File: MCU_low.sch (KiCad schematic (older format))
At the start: 20 parts

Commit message: - MCU_Low: added encoder, DAC, alternate MCU
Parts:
- removed SW?: Rotary_Encoder_Switch, symbol Device:Rotary_Encoder_Switch
- added SW?: Rotary_Encoder_Switch, Rotary_Encoder:RotaryEncoder_Alps_EC12E-Switch_Vertical_H20mm_CircularMountingHoles, symbol Device:Rotary_Encoder_Switch
- added U?: LCD_I2C, symbol miscellaneous:LCD_I2C
- added U?: STM32F103C8Tx, Package_QFP:LQFP-48_7x7mm_P0.5mm, symbol MCU_ST_STM32F1:STM32F103C8Tx
- added U?: DAC8564, Package_SO:TSSOP-16_4.4x5mm_P0.65mm, symbol miscellaneous:DAC8564
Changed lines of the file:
@@
 $EndDescr
-$Comp
-L Device:Rotary_Encoder_Switch SW?
-U 1 1 5F7D692F
-P 2400 6850
-AR Path="/5F7D692F" Ref="SW?"  Part="1"
-AR Path="/5F7D6767/5F7D692F" Ref="SW?"  Part="1"
-F 0 "SW?" H 2400 7217 50  0000 C CNN
-F 1 "Rotary_Encoder_Switch" H 2400 7126 50  0000 C CNN
-F 2 "" H 2250 7010 50  0001 C CNN
-F 3 "~" H 2400 7110 50  0001 C CNN
-	1    2400 6850
-	1    0    0    -1
-$EndComp
 $Comp
 L MCU_Module:NUCLEO64-F411RE U?
@@
 $EndComp
 Connection ~ 8450 5300
+$Comp
+L miscellaneous:LCD_I2C U?
+U 1 1 5F8792B9
+P 8950 1200
+F 0 "U?" H 9579 1246 50  0000 L CNN
+F 1 "LCD_I2C" H 9579 1155 50  0000 L CNN
+F 2 "" H 8950 1200 50  0001 C CNN
+F 3 "" H 8950 1200 50  0001 C CNN
+	1    8950 1200
+	1    0    0    -1
+$EndComp
+$Comp
+L power:GND #PWR?
+U 1 1 5F879504
+P 8550 1500
+AR Path="/5F40DCB9/5F879504" Ref="#PWR?"  Part="1"
+AR Path="/5F618AB9/5F879504" Ref="#PWR?"  Part="1"
+AR Path="/5F879504" Ref="#PWR?"  Part="1"
+AR Path="/5F620813/5F879504" Ref="#PWR?"  Part="1"
+AR Path="/5F7D6767/5F879504" Ref="#PWR?"  Part="1"
+F 0 "#PWR?" H 8550 1340 50  0001 C CNN
+F 1 "GND" H 8550 1400 39  0000 C TNN
+F 2 "" H 8550 1500 50  0001 C CNN
+F 3 "" H 8550 1500 50  0001 C CNN
+	1    8550 1500
+	1    0    0    -1
+$EndComp
+$Comp
+L Device:Rotary_Encoder_Switch SW?
+U 1 1 5F87AEF8
+P 7700 1200
+AR Path="/5F87AEF8" Ref="SW?"  Part="1"
+AR Path="/5F7D6767/5F87AEF8" Ref="SW?"  Part="1"
+F 0 "SW?" H 7700 1567 50  0000 C CNN
+F 1 "Rotary_Encoder_Switch" H 7700 1476 50  0000 C CNN
+F 2 "Rotary_Encoder:RotaryEncoder_Alps_EC12E-Switch_Vertical_H20mm_CircularMountingHoles" H 7550 1360 50  0001 C CNN
+F 3 "~" H 7700 1460 50  0001 C CNN
+F 4 "PEC12R-4222F-S0024" H 7700 1200 50  0001 C CNN "Mfr. No"
+F 5 "4.33" H 7700 1200 50  0001 C CNN "Price [PLN]"
+	1    7700 1200
+	1    0    0    -1
+$EndComp
+$Comp
+L MCU_ST_STM32F1:STM32F103C8Tx U?
+U 1 1 5F87E496
+P 3050 2950
+F 0 "U?" H 3000 1364 50  0000 C CNN
+F 1 "STM32F103C8Tx" H 3000 1273 50  0000 C CNN
+F 2 "Package_QFP:LQFP-48_7x7mm_P0.5mm" H 2450 1550 50  0001 R CNN
+F 3 "http://www.st.com/st-web-ui/static/active/en/resource/technical/document/datasheet/CD00161566.pdf" H 3050 2950 50  0001 C CNN
+	1    3050 2950
+	1    0    0    -1
+$EndComp
+$Comp
+L miscellaneous:DAC8564 U?
+U 1 1 5F888149
+P 5500 6750
+F 0 "U?" H 5500 5814 50  0000 C CNN
+F 1 "DAC8564" H 5500 5723 50  0000 C CNN
+F 2 "Package_SO:TSSOP-16_4.4x5mm_P0.65mm" H 6500 5700 50  0001 C CNN
+F 3 "" H 6500 5700 50  0001 C CNN
+F 4 "44.7" H 5500 6750 50  0001 C CNN "Price [PLN]"
+	1    5500 6750
+	1    0    0    -1
+$EndComp
 $EndSCHEMATC

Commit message: - drivers modified - MCU replaced
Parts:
- removed C? (x7): 100n, Capacitor_SMD:C_0603_1608Metric_Pad1.05x0.95mm_HandSolder, symbol Device:C_Small
- removed U?: NUCLEO64-F411RE, Module:ST_Morpho_Connector_144_STLink, symbol MCU_Module:NUCLEO64-F411RE
- removed U?: STM32F103C8Tx, Package_QFP:LQFP-48_7x7mm_P0.5mm, symbol MCU_ST_STM32F1:STM32F103C8Tx
- removed U?: DAC8564, Package_SO:TSSOP-16_4.4x5mm_P0.65mm, symbol miscellaneous:DAC8564
- added C? (x7): 10n, Capacitor_SMD:C_0603_1608Metric_Pad1.05x0.95mm_HandSolder, symbol Device:C_Small
- added U?: STM32L431RBTx, Package_QFP:LQFP-64_10x10mm_P0.5mm, symbol MCU_ST_STM32L4:STM32L431RBTx
- C?: value 100n -> 10n
- SW?: footprint Rotary_Encoder:RotaryEncoder_Alps_EC12E-Switch_Vertical_H20mm_CircularMountingHoles -> miscellaneous_my:Encoder_12.4x13.4_pitch2.5mm_wSw
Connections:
- net labels added: +3V3, TIM1_CH1, TIM1_CH2, TIM1_CH3, TIM1_CH4, dac_1, dac_2, dac_3, dac_4
- net labels removed: dac_E, dac_F, dac_K
- wire segments 34 -> 58
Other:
- moved on the sheet: C?, R?

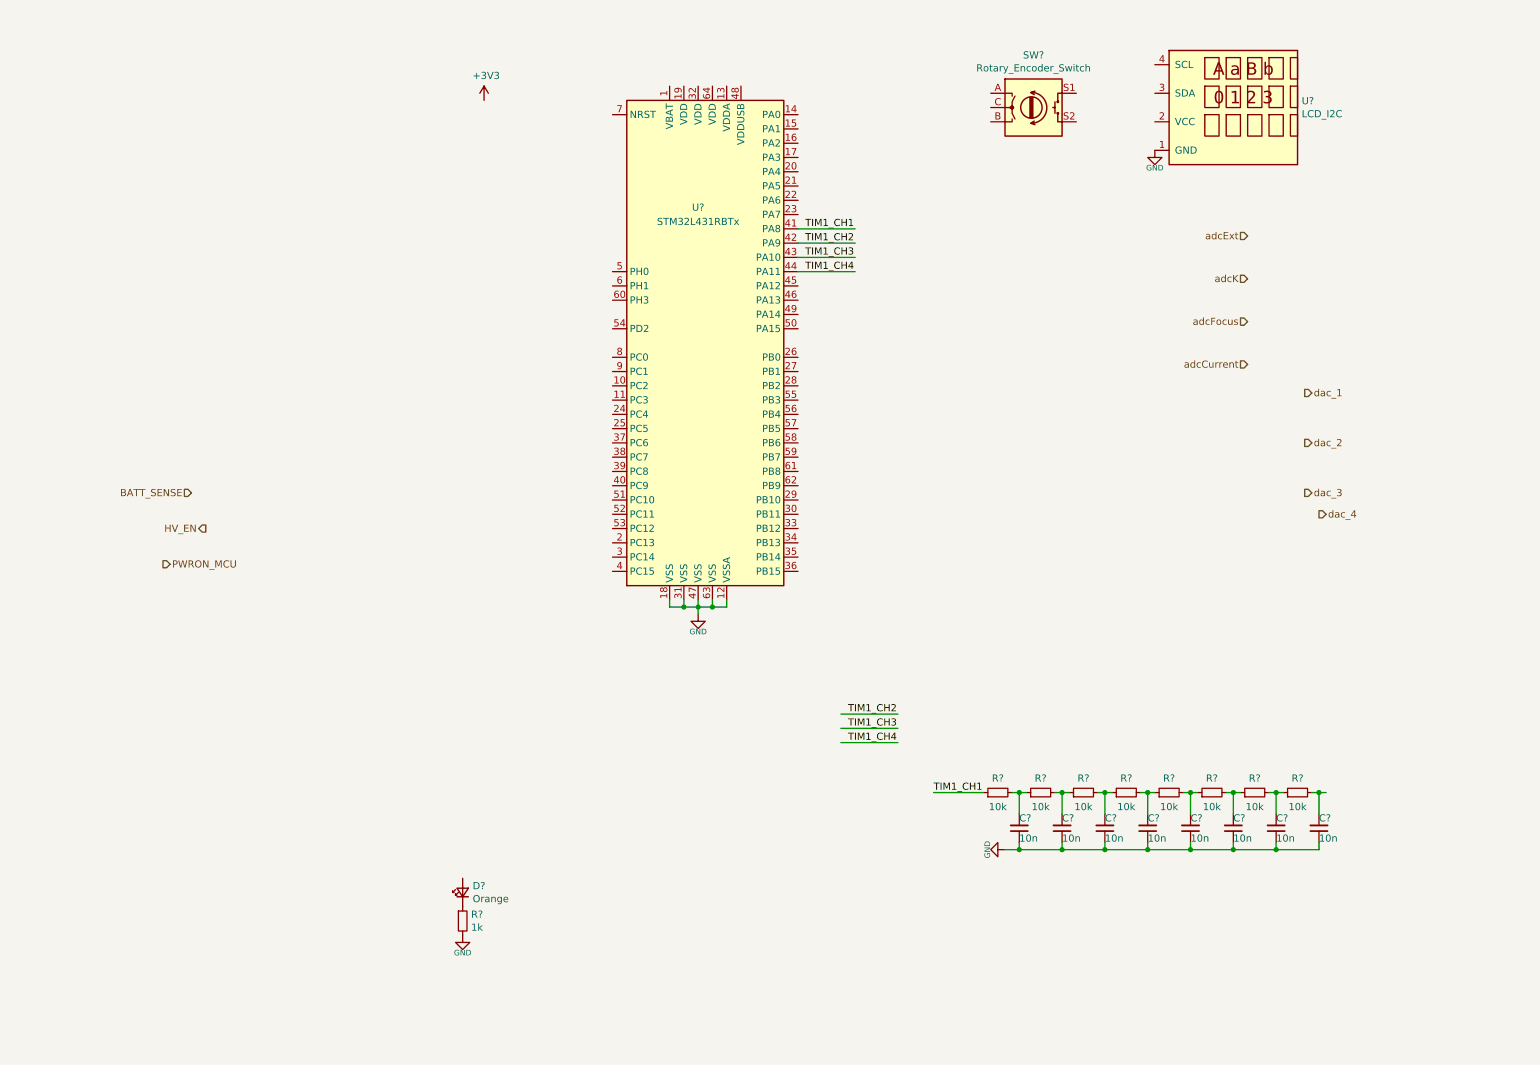
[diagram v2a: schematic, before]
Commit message: - connect things to MCUlow (DAC, screen, keys, debug) - improvement in charger (read PWR key)
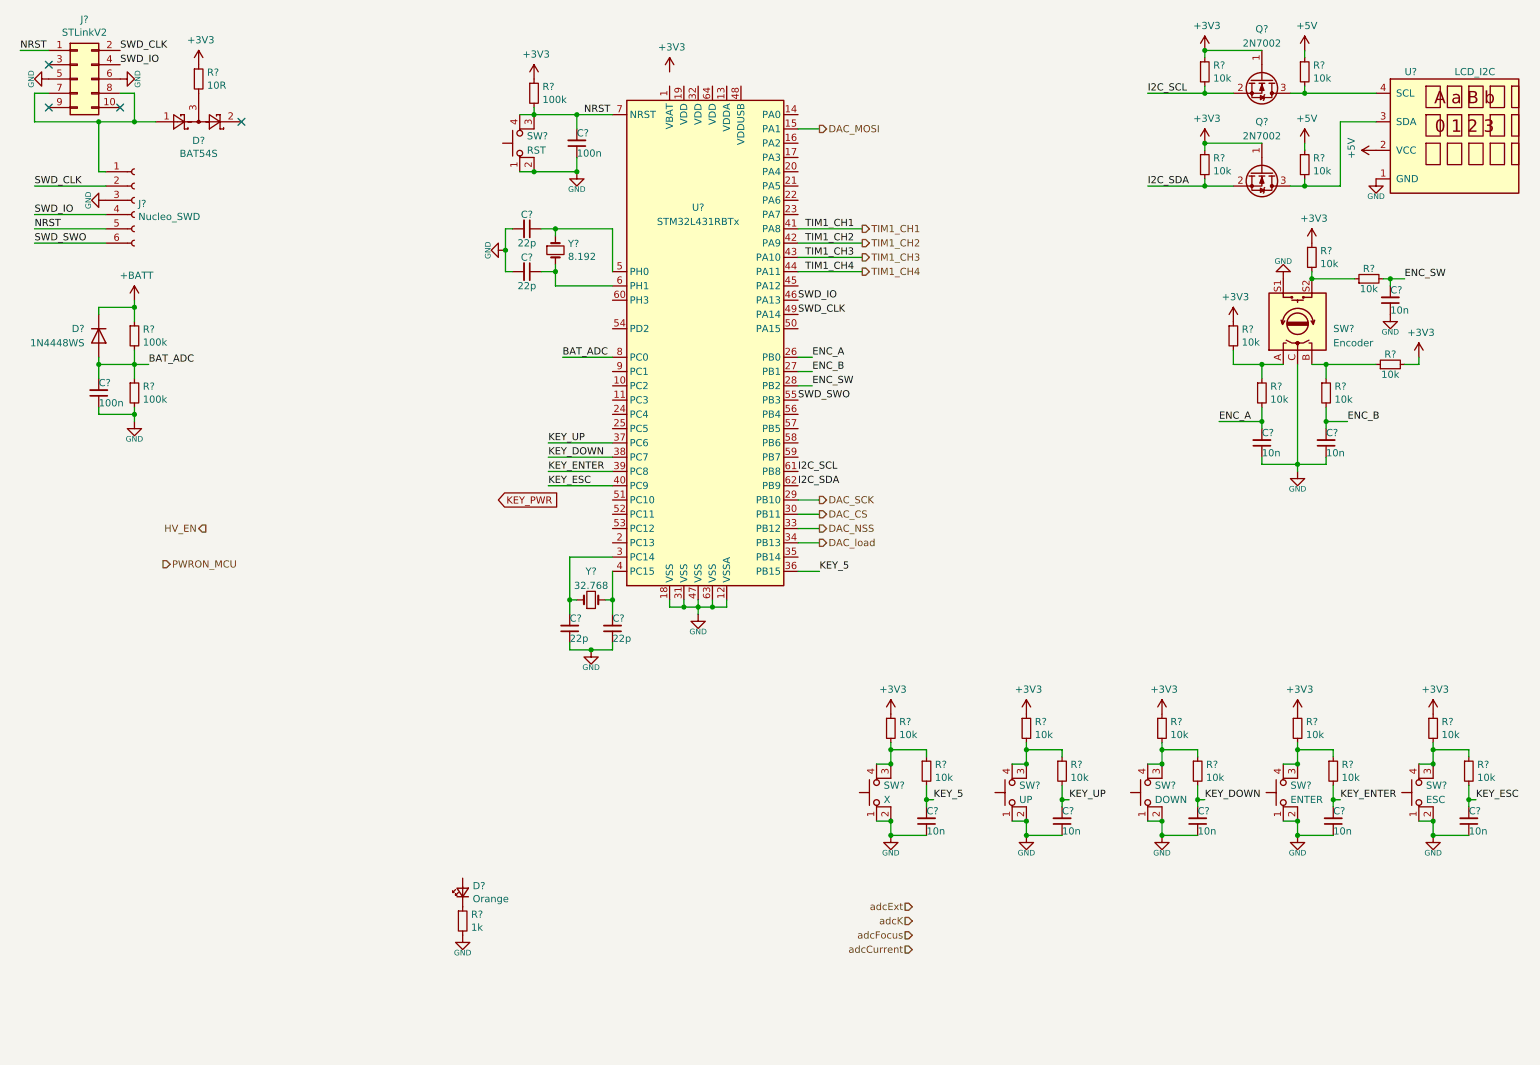
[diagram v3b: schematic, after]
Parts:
- removed C? (x8): 10n, Capacitor_SMD:C_0603_1608Metric_Pad1.05x0.95mm_HandSolder, symbol Device:C_Small
- removed R? (x8): 10k, Resistor_SMD:R_0603_1608Metric_Pad1.05x0.95mm_HandSolder, symbol Device:R_Small
- added C? (x2): 100n, Capacitor_SMD:C_0603_1608Metric_Pad1.05x0.95mm_HandSolder, symbol Device:C_Small
- added C? (x4): 22p, Capacitor_SMD:C_0603_1608Metric_Pad1.05x0.95mm_HandSolder, symbol Device:C_Small
- added C? (x8): 10n, Capacitor_SMD:C_0603_1608Metric_Pad1.05x0.95mm_HandSolder, symbol Device:C_Small
- added D?: BAT54S, Package_TO_SOT_SMD:SOT-23, symbol Diode:BAT54S
- added D?: 1N4448WS, Diode_SMD:D_SOD-323, symbol Diode:1N4448WS
- added J?: STLinkV2, miscellaneous_my:ST-LinkV2_FakeStm8Stm32_vertical, symbol Connector_Generic:Conn_02x05_Odd_Even
- added J?: Nucleo_SWD, Connector_PinSocket_2.54mm:PinSocket_1x06_P2.54mm_Vertical, symbol Connector:Conn_01x06_Female
- added Q? (x2): 2N7002, Package_TO_SOT_SMD:SOT-23, symbol Transistor_FET:2N7002
- added R?: 10R, Resistor_SMD:R_0603_1608Metric_Pad1.05x0.95mm_HandSolder, symbol Device:R_Small
- added R? (x3): 100k, Resistor_SMD:R_0603_1608Metric_Pad1.05x0.95mm_HandSolder, symbol Device:R_Small
- added R? (x20): 10k, Resistor_SMD:R_0603_1608Metric_Pad1.05x0.95mm_HandSolder, symbol Device:R_Small
- added SW?: RST, Button_Switch_SMD:SW_Push_1P1T_NO_6x6mm_H9.5mm, symbol Switch:SW_MEC_5E
- added SW?: ESC, Button_Switch_SMD:SW_Push_1P1T_NO_6x6mm_H9.5mm, symbol Switch:SW_MEC_5E
- added SW?: ENTER, Button_Switch_SMD:SW_Push_1P1T_NO_6x6mm_H9.5mm, symbol Switch:SW_MEC_5E
- added SW?: UP, Button_Switch_SMD:SW_Push_1P1T_NO_6x6mm_H9.5mm, symbol Switch:SW_MEC_5E
- added SW?: DOWN, Button_Switch_SMD:SW_Push_1P1T_NO_6x6mm_H9.5mm, symbol Switch:SW_MEC_5E
- added SW?: X, Button_Switch_SMD:SW_Push_1P1T_NO_6x6mm_H9.5mm, symbol Switch:SW_MEC_5E
- added Y?: 8.192, Crystal:Crystal_HC49-4H_Vertical, symbol Device:Crystal_Small
- added Y?: 32.768, Crystal:Crystal_AT310_D3.0mm_L10.0mm_Horizontal_1EP_style2, symbol Device:Crystal_Small
- SW?: value Rotary_Encoder_Switch -> Encoder
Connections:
- net labels added: +5V, +BATT, BAT_ADC, DAC_CS, DAC_MOSI, DAC_NSS, DAC_SCK, DAC_load, ENC_A, ENC_B, ENC_SW, I2C_SCL, I2C_SDA, KEY_5, KEY_DOWN, KEY_ENTER, KEY_ESC, KEY_PWR, KEY_UP, NRST, SWD_CLK, SWD_IO, SWD_SWO
- net labels removed: BATT_SENSE, dac_1, dac_2, dac_3, dac_4
- wire segments 58 -> 188
- no-connect marks 0 -> 4
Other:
- moved on the sheet: SW?, U?

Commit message: - high side (supply, MCU) - low side MCU - much small changes
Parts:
- removed D?: BAT54S, Package_TO_SOT_SMD:SOT-23, symbol Diode:BAT54S
- removed J?: STLinkV2, miscellaneous_my:ST-LinkV2_FakeStm8Stm32_vertical, symbol Connector_Generic:Conn_02x05_Odd_Even
- removed J?: Nucleo_SWD, Connector_PinSocket_2.54mm:PinSocket_1x06_P2.54mm_Vertical, symbol Connector:Conn_01x06_Female
- removed R?: 10R, Resistor_SMD:R_0603_1608Metric_Pad1.05x0.95mm_HandSolder, symbol Device:R_Small
- added C? (x5): 100n, Capacitor_SMD:C_0603_1608Metric_Pad1.05x0.95mm_HandSolder, symbol Device:C_Small
- added C? (x2): 22p, Capacitor_SMD:C_0603_1608Metric_Pad1.05x0.95mm_HandSolder, symbol Device:C_Small
- added C?: 1u, Capacitor_SMD:C_0603_1608Metric_Pad1.05x0.95mm_HandSolder, symbol Device:C_Small
- added D?: RB520S30, miscellaneous_my:D_SOD-323-523_HandSoldering, symbol Device:D_Schottky_Small
- added J?: STLinkV2, miscellaneous_my:ST-LinkV2_FakeStm8Stm32_vertical, symbol Connector_Generic:Conn_02x05_Odd_Even
- added J?: Nucleo_SWD, Connector_PinSocket_2.54mm:PinSocket_1x06_P2.54mm_Vertical, symbol Connector:Conn_01x06_Female
- added L? (x2): BLM18TG102, Resistor_SMD:R_0603_1608Metric_Pad1.05x0.95mm_HandSolder, symbol Device:L_Core_Ferrite_Small
- added R?: 0R, Resistor_SMD:R_0603_1608Metric_Pad1.05x0.95mm_HandSolder, symbol Device:R_Small
- added R?: 10R, Resistor_SMD:R_0603_1608Metric_Pad1.05x0.95mm_HandSolder, symbol Device:R_Small
- added U?: ADS131M06, miscellaneous_my:TQFP-32_5x5mm_P0.5mm_edges, symbol miscellaneous:ADS131M06
- added Y?: 8.192, Crystal:Crystal_AT310_D3.0mm_L10.0mm_Horizontal_1EP_style2, symbol Device:Crystal_Small
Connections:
- net +3V3: now also C?.1, L?.1, R?.1, U?.26 (DVDD)
- net DAC_MOSI: now also U?.11 (PC3); no longer U?.15 (PA1)
- net DAC_load: now also U?.25 (PC5); no longer U?.34 (PB13)
- net GND: now also C?.2, C?.2, C?.2, C?.2, C?.2, C?.2, C?.2, C?.2, J?.3 (Pin_3), J?.5 (Pin_5), J?.6 (Pin_6), U?.13 (AGND), U?.25 (DGND), U?.28 (AGND)
- net KEY_PWR: now also U?.35 (PB14)
- net NRST: now also J?.5 (Pin_5), J?.9 (Pin_9)
- net SWD_CLK: now also J?.2 (Pin_2), J?.2 (Pin_2)
- net SWD_IO: now also J?.4 (Pin_4), J?.4 (Pin_4)
- net SWD_SWO: now also J?.6 (Pin_6), J?.7 (Pin_7)
- net TIM1_CH1: now also U?.34 (PB13); no longer U?.41 (PA8)
- net ADC_RESET: now reaches U?.20 (PA4)
- net ADC_RESET: now also U?.16 (~SYNC~/~RESET)
- net ADC_CS: now reaches U?.21 (PA5)
- net ADC_CS: now also U?.17 (~CS)
- net ADC_MISO: now reaches U?.22 (PA6)
- net ADC_MISO: now also U?.20 (DOUT)
- net ADC_MOSI: now reaches U?.23 (PA7)
- net ADC_MOSI: now also U?.21 (DIN)
- net ADC_DRDY: now reaches U?.24 (PC4)
- net ADC_DRDY: now also U?.18 (~DRDY)
- net PWRON_LOCK: now reaches U?.45 (PA12)
- new net: C?.1, U?.24 (CAP)
- new net: C?.1, L?.1, L?.2
- new net: C?.1, C?.1, L?.2, U?.15 (AVDD)
- new net: C?.1, U?.14 (REFIN)
- new net: C?.1, U?.22 (XTAL2), Y?.2
- new net: C?.1, R?.1, U?.23 (XTAL1/CLKIN), Y?.1
- new net: D?.2 (A), J?.1 (Pin_1), J?.8 (Pin_8)
- new net: D?.1 (K), R?.2
- new net ADC_SCK: U?.15 (PA1), U?.19 (SCLK)
- new net MCO: R?.2, U?.41 (PA8)
- no-connect marks 4 -> 3
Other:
- moved on the sheet: C?, D?, R?, SW?, U?, Y?

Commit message: - final schematic
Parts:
- added C118, C119, C120, C121, C122: 100n, Capacitor_SMD:C_0603_1608Metric_Pad1.05x0.95mm_HandSolder, symbol Device:C_Small
- added C137, C138, C139, C140, C146, C147: 1n, Capacitor_SMD:C_0603_1608Metric_Pad1.05x0.95mm_HandSolder, symbol Device:C_Small
- added D25: Orange, Diode_SMD:D_0805_2012Metric_Pad1.15x1.40mm_HandSolder, symbol Device:LED_Small
- added D26: Red, Diode_SMD:D_0805_2012Metric_Pad1.15x1.40mm_HandSolder, symbol Device:LED_Small
- added D27: Blue, Diode_SMD:D_0805_2012Metric_Pad1.15x1.40mm_HandSolder, symbol Device:LED_Small
- added R127, R146, R148, R154, R160, R161, R162: 0R, Resistor_SMD:R_0603_1608Metric_Pad1.05x0.95mm_HandSolder, symbol Device:R_Small
- added R140, R141, R142: 1k, Resistor_SMD:R_0603_1608Metric_Pad1.05x0.95mm_HandSolder, symbol Device:R_Small
- added TP16, TP17, TP18, TP19: TestPoint, TestPoint:TestPoint_THTPad_D1.5mm_Drill0.7mm, symbol Connector:TestPoint
- D24: renamed from D?; value Orange -> Green
- Q15, Q16: renamed from Q?; value 2N7002 -> BSS138
- gave numbers to parts that had none: 67
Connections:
- net +3V3: now also U26.13 (VDDA), U26.19 (VDD), U26.32 (VDD), U26.48 (VDDUSB), U26.64 (VDD), C118.2, C119.2, C120.2, C121.2, C122.2, R127.2
- net GND: now also U27.2 (AIN2N), U27.3 (AIN3N), U27.30 (AIN0N), U27.31 (AIN1N), U27.6 (AIN4N), U27.7 (AIN5N), C118.1, C119.1, C120.1, C121.1, C122.1, C137.1, C138.1, C139.1, C140.1, C146.1, C147.1, R140.2, R141.2, R142.2
- net LED_GRN: now reaches D24.2 (A)
- net LED_GRN: now also U26.51 (PC10)
- net at U26.1 (VBAT): now also R127.1
- net LED_BLU: now reaches U26.50 (PA15)
- net LED_BLU: now also D27.2 (A)
- net LED_ORG: now reaches U26.52 (PC11)
- net LED_ORG: now also D25.2 (A)
- net LED_RED: now reaches U26.53 (PC12)
- net LED_RED: now also D26.2 (A)
- net UART_TX: now reaches U26.58 (PB6)
- net UART_RX: now reaches U26.59 (PB7)
- net at U27.1 (AIN2P): now also C139.2, R154.2
- net at U27.29 (AIN0P): now also C137.2, R146.2
- net at U27.32 (AIN1P): now also C138.2, R148.2
- net at U27.4 (AIN3P): now also C140.2, R160.2
- net at U27.5 (AIN4P): now also C146.2, R161.2
- net at U27.8 (AIN5P): now also C147.2, R162.2
- net PWRON_LOCK renamed PWR_LOCK
- new net: D25.1 (K), R140.1
- new net: D26.1 (K), R141.1
- new net: D27.1 (K), R142.1
- new net: R162.1, TP19.1
- new net: R161.1, TP18.1
- new net: R160.1, TP17.1
- new net: R154.1, TP16.1
- new net ADC_CH0: R146.1
- new net ADC_CH1: R148.1
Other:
- moved on the sheet: D24, R139

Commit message: - init PCB - fix last things in schematic
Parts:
- removed SW10: ESC, Button_Switch_SMD:SW_Push_1P1T_NO_6x6mm_H9.5mm, symbol Switch:SW_MEC_5E
- removed SW4: RST, Button_Switch_SMD:SW_Push_1P1T_NO_6x6mm_H9.5mm, symbol Switch:SW_MEC_5E
- removed SW6: X, Button_Switch_SMD:SW_Push_1P1T_NO_6x6mm_H9.5mm, symbol Switch:SW_MEC_5E
- removed SW7: UP, Button_Switch_SMD:SW_Push_1P1T_NO_6x6mm_H9.5mm, symbol Switch:SW_MEC_5E
- removed SW8: DOWN, Button_Switch_SMD:SW_Push_1P1T_NO_6x6mm_H9.5mm, symbol Switch:SW_MEC_5E
- removed SW9: ENTER, Button_Switch_SMD:SW_Push_1P1T_NO_6x6mm_H9.5mm, symbol Switch:SW_MEC_5E
- added SW10: ESC, Button_Switch_SMD:SW_Push_1P1T_NO_6x6mm_H9.5mm, symbol Switch:SW_Push
- added SW4: RST, Button_Switch_SMD:SW_Push_1P1T_NO_6x6mm_H9.5mm, symbol Switch:SW_Push
- added SW6: X, Button_Switch_SMD:SW_Push_1P1T_NO_6x6mm_H9.5mm, symbol Switch:SW_Push
- added SW7: UP, Button_Switch_SMD:SW_Push_1P1T_NO_6x6mm_H9.5mm, symbol Switch:SW_Push
- added SW8: DOWN, Button_Switch_SMD:SW_Push_1P1T_NO_6x6mm_H9.5mm, symbol Switch:SW_Push
- added SW9: ENTER, Button_Switch_SMD:SW_Push_1P1T_NO_6x6mm_H9.5mm, symbol Switch:SW_Push
- added TP25, TP26, TP27, TP28, TP29, TP30, TP31, TP32: TestPoint, TestPoint:TestPoint_THTPad_D1.5mm_Drill0.7mm, symbol Connector:TestPoint
- U25: footprint (none) -> miscellaneous_my:HD44780_20x4_wPCF8574
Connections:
- net GND: now also SW10.1, SW4.1, SW6.1, SW7.1, SW8.1, SW9.1
- net NRST: now also SW4.2
- net at U26.10 (PC2): now also TP30.1
- net at U26.14 (PA0): now also TP25.1
- net at U26.16 (PA2): now also TP26.1
- net at U26.17 (PA3): now also TP27.1
- net at U26.54 (PD2): now also TP28.1
- net at U26.56 (PB4): now also TP31.1
- net at U26.57 (PB5): now also TP32.1
- net at U26.9 (PC1): now also TP29.1
- net at R153.2, R159.1: now also SW10.2
- net at R152.2, R158.1: now also SW9.2
- net at R150.2, R156.1: now also SW7.2
- net at R151.2, R157.1: now also SW8.2
- net at R149.2, R155.1: now also SW6.2

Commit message: - pcb placement, add 3dShapes
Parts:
- Y3: footprint Crystal:Crystal_AT310_D3.0mm_L10.0mm_Horizontal_1EP_style2 -> Crystal:Crystal_HC49-4H_Vertical
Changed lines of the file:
@@
 F 0 "Y3" H 3600 5250 50  0000 C CNN
 F 1 "8.192" H 3600 5150 50  0000 C CNN
-F 2 "Crystal:Crystal_AT310_D3.0mm_L10.0mm_Horizontal_1EP_style2" H 3600 5050 50  0001 C CNN
+F 2 "Crystal:Crystal_HC49-4H_Vertical" H 3600 5050 50  0001 C CNN
 F 3 "~" H 3600 5050 50  0001 C CNN
 	1    3600 5050

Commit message: - PCB progress
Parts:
- removed R127: 0R, Resistor_SMD:R_0603_1608Metric_Pad1.05x0.95mm_HandSolder, symbol Device:R_Small
- C117, C118, C119, C120, C121, C122, C123, C124, C125, C126, C127, C128, C129, C130, C131, C132, C133, C134, C135, C136, C137, C138, C139, C140, C141, C142, C143, C144, C145, C146, C147, C148, C149: footprint Capacitor_SMD:C_0603_1608Metric_Pad1.05x0.95mm_HandSolder -> Capacitor_SMD:C_0603_1608Metric
- L12, L13: footprint Resistor_SMD:R_0603_1608Metric_Pad1.05x0.95mm_HandSolder -> Inductor_SMD:L_0603_1608Metric
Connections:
- net +3V3: now also U26.1 (VBAT)
